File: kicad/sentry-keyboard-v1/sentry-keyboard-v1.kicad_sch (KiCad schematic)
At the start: 273 parts, among them J1 USB_C_Receptacle_USB2.0, J4 AVR-ISP-6, SW1 Reset, SW2 RotaryEncoder_Switch, U1 ATmega32U4-AU, U3 PRTR5V0U2X, Y1 16Mhz

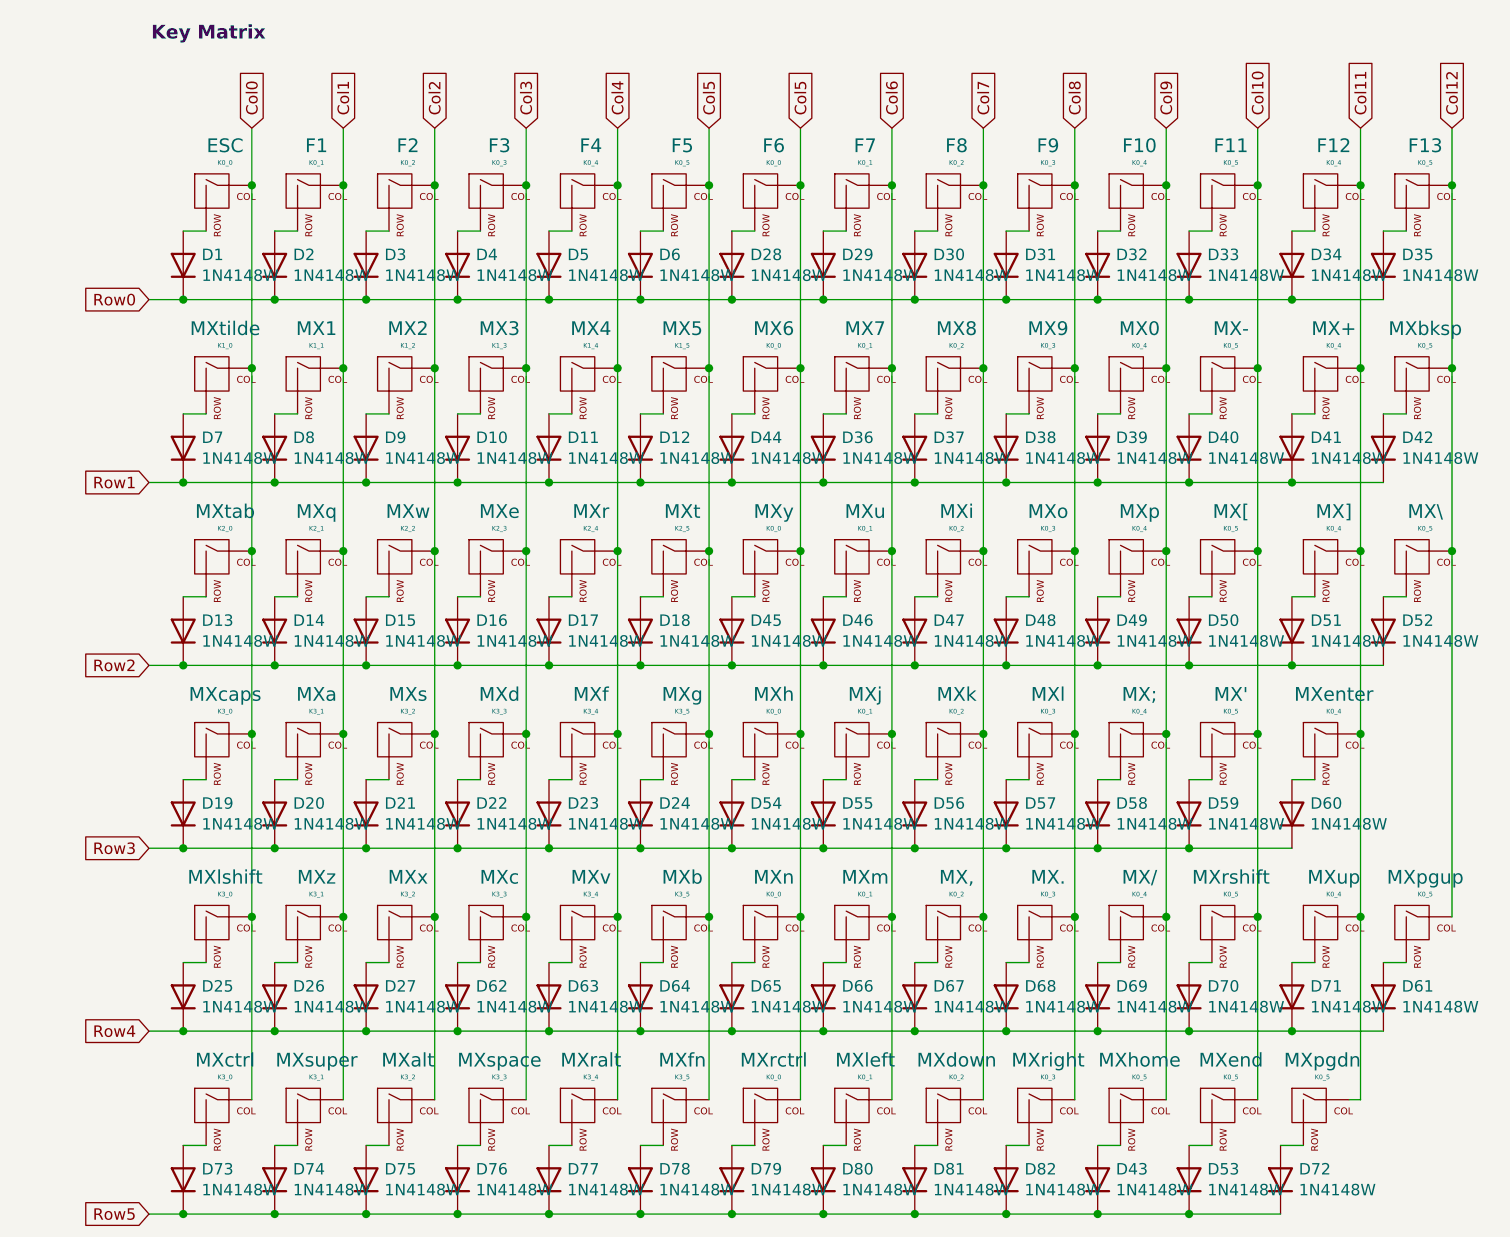
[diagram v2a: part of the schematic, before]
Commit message: Assign footprints
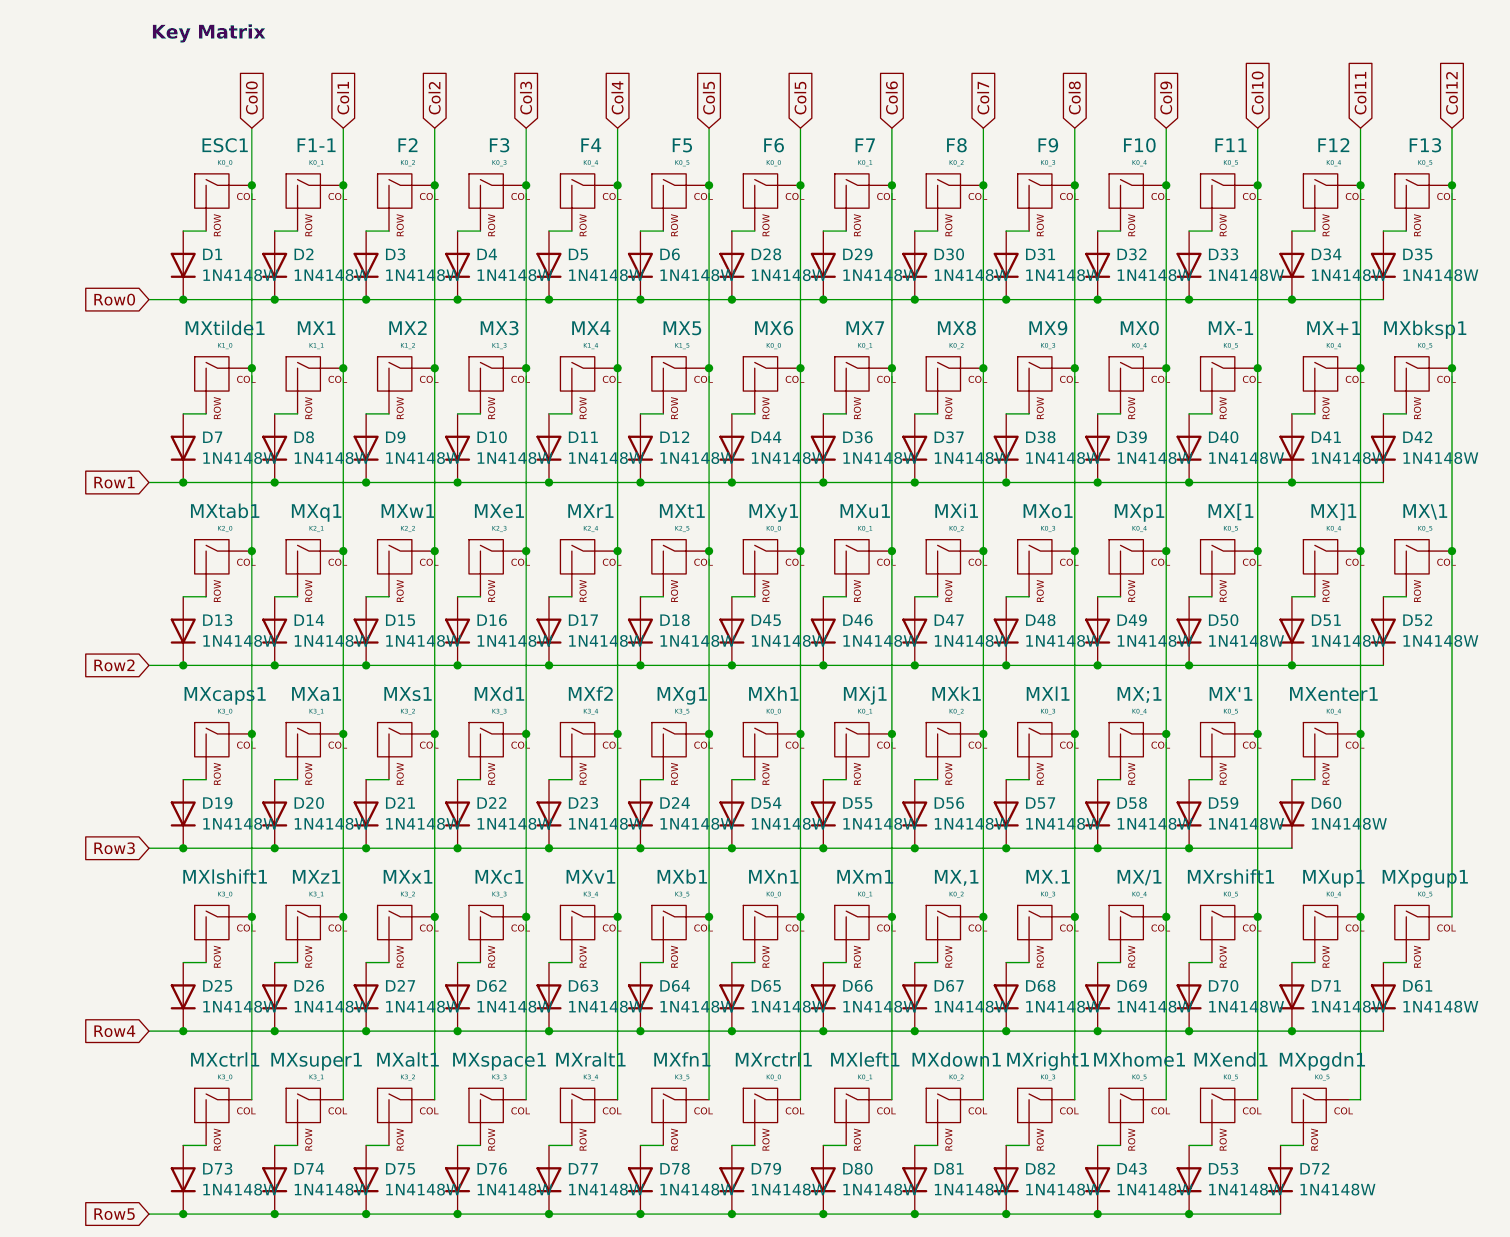
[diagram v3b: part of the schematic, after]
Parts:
- C8, C9: footprint (none) -> Capacitor_SMD:C_0805_2012Metric
- R10, R6, R7, R9: footprint (none) -> Resistor_SMD:R_0805_2012Metric
- SW2: footprint (none) -> Rotary_Encoder:RotaryEncoder_Alps_EC11E-Switch_Vertical_H20mm_MountingHoles
- renumbered ESC to ESC1, F1 to F1-1, MX' to MX'1, MX+ to MX+1, MX, to MX,1, MX- to MX-1, MX. to MX.1, MX/ to MX/1, MX; to MX;1, MX[ to MX[1, MX\ to MX\1, MX] to MX]1, MXa to MXa1, MXalt to MXalt1, MXb to MXb1, MXbksp to MXbksp1, MXc to MXc1, MXcaps to MXcaps1, MXctrl to MXctrl1, MXd to MXd1, MXdown to MXdown1, MXe to MXe1, MXend to MXend1, MXenter to MXenter1, MXf to MXf2, MXfn to MXfn1, MXg to MXg1, MXh to MXh1, MXhome to MXhome1, MXi to MXi1, MXj to MXj1, MXk to MXk1, MXl to MXl1, MXleft to MXleft1, MXlshift to MXlshift1, MXm to MXm1, MXn to MXn1, MXo to MXo1, MXp to MXp1, MXpgdn to MXpgdn1, MXpgup to MXpgup1, MXq to MXq1, MXr to MXr1, MXralt to MXralt1, MXrctrl to MXrctrl1, MXright to MXright1, MXrshift to MXrshift1, MXs to MXs1, MXspace to MXspace1, MXsuper to MXsuper1, MXt to MXt1, MXtab to MXtab1, MXtilde to MXtilde1, MXu to MXu1, MXup to MXup1, MXv to MXv1, MXw to MXw1, MXx to MXx1, MXy to MXy1, MXz to MXz1
